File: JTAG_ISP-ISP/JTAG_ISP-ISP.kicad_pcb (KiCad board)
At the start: 2 copper layers, 23.1 x 45.1 mm, 5 parts, among them J1 Conn_02x03_Counter_Clockwise, J2 Conn_01x08, J3 Conn_01x08

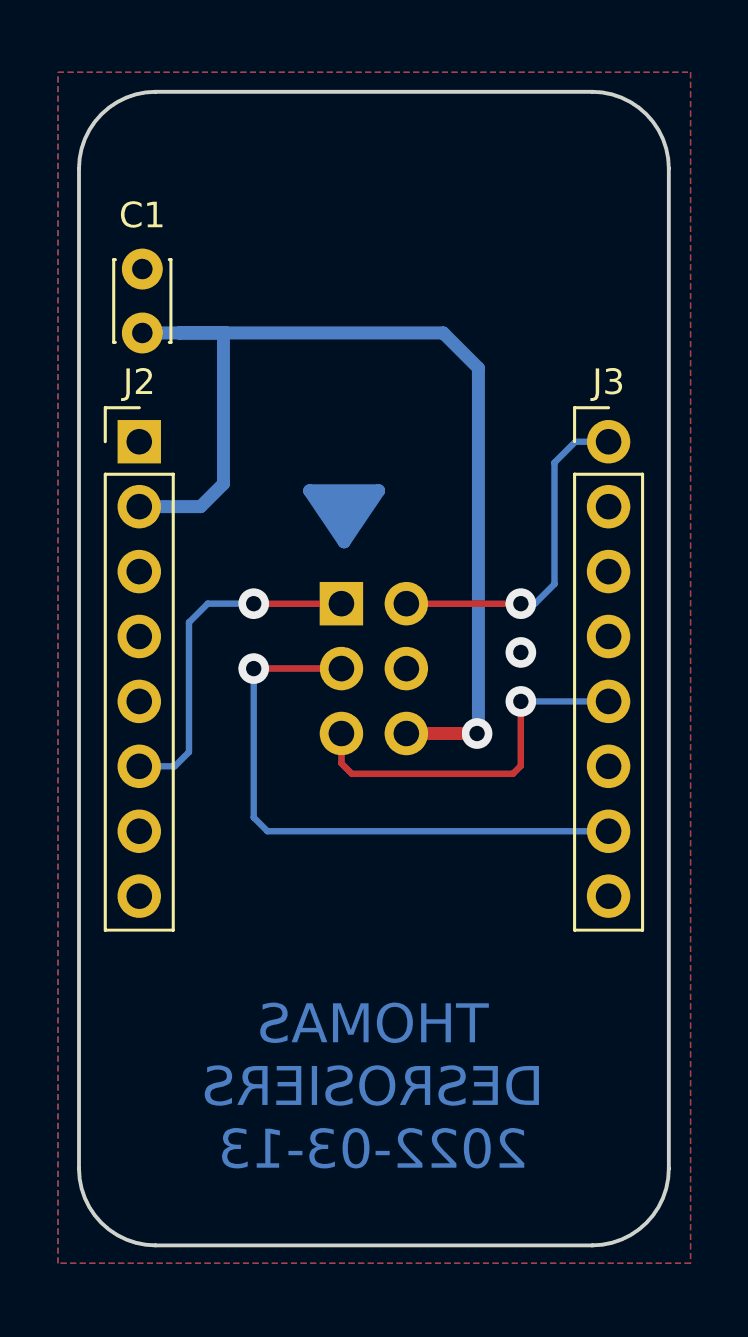
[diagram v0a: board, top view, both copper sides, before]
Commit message: + Ajout d'un trou sur chacun des 2 PCB pour pouvoir y fixer une dragone. + Ajout d'un espace de texte contenant mon nom et la date sur le PCB ISP. + Ajout d'un dossier contenant les fichiers générés pour panélisation par une application externe à KiCad. **Le circuit pour l'étage ISP est à vérifier**
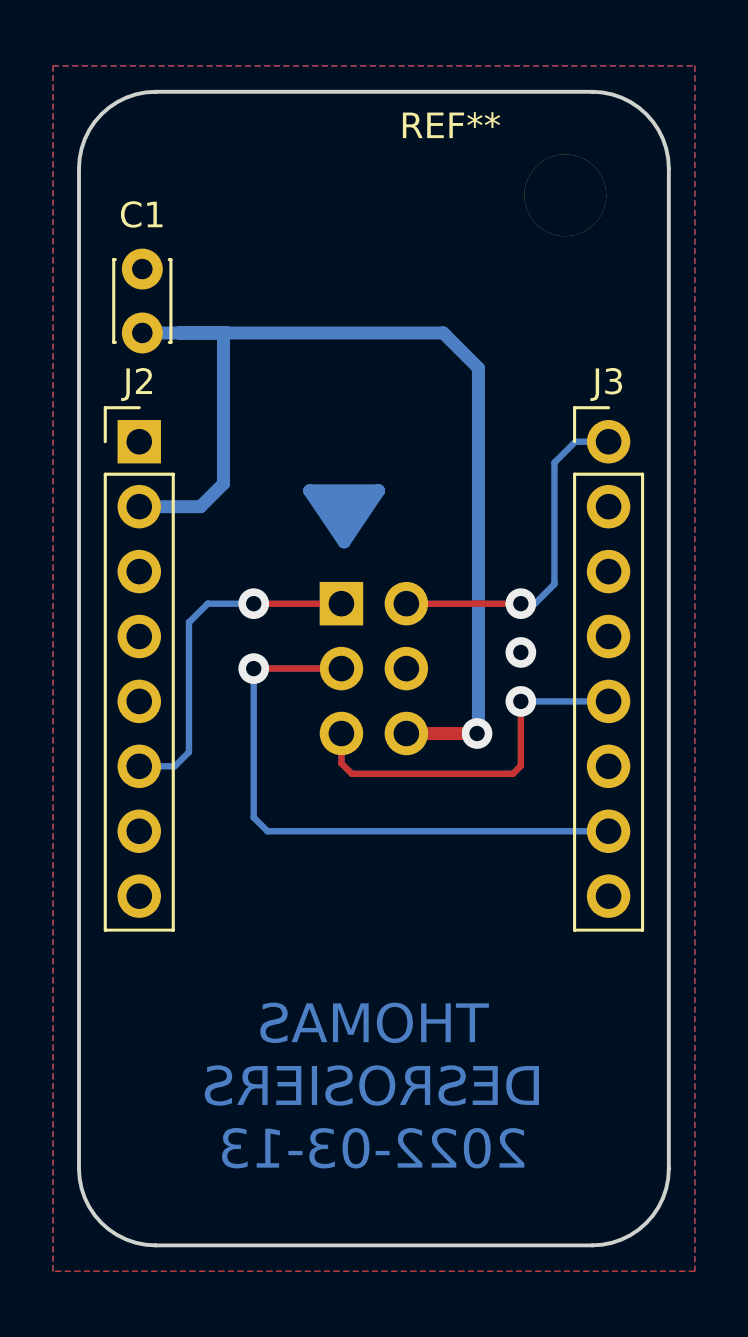
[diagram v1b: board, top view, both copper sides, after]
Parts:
- added REF**: MountingHole_3.2mm_M3, MountingHole:MountingHole_3.2mm_M3, F.Cu at (163.8, 65.9)
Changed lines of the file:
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@@
     )
     (pad_to_mask_clearance 0)
+    (aux_axis_origin 143.806012 60.797592)
+    (grid_origin 143.806012 60.797592)
     (pcbplotparams
       (layerselection 0x0001000_ffffffff)
@@
     )
   )
+  (footprint "MountingHole:MountingHole_3.2mm_M3" (layer "F.Cu")
+    (at 163.85 65.86358)
+    (descr "Mounting Hole 3.2mm, no annular, M3")
+    (tags "mounting hole 3.2mm no annular m3")
+    (attr exclude_from_pos_files exclude_from_bom)
+    (fp_text reference "REF**" (at -4.500012 -2.699989) (layer "F.SilkS")
+      (effects (font (size 1 1) (thickness 0.15)))
+    )
+    (fp_text value "MountingHole_3.2mm_M3" (at 0 4.2) (layer "F.Fab")
+      (effects (font (size 1 1) (thickness 0.15)))
+    )
+    (fp_text user "${REFERENCE}" (at -4.500012 -2.699989) (layer "F.Fab")
+      (effects (font (size 1 1) (thickness 0.15)))
+    )
+    (fp_circle (center 0 0) (end 3.2 0) (layer "Cmts.User") (width 0.15) (fill none))
+    (fp_circle (center 0 0) (end 3.45 0) (layer "F.CrtYd") (width 0.05) (fill none))
+    (pad "" thru_hole circle locked (at 0 0) (size 3.200001 3.200001) (drill 3.200001) (layers *.Cu *.Mask))
+  )
   (footprint "Connector_PinHeader_2.54mm:PinHeader_1x08_P2.54mm_Vertical" (layer "F.Cu")
     (at 165.542011 75.505767)
@@
   (gr_arc (start 167.9 103.95) (mid 167.02132 106.07132) (end 164.9 106.95) (layer "Edge.Cuts") (width 0.15))
   (gr_rect (start 167.9 61.81358) (end 144.822002 106.95) (layer "User.1") (width 1.016) (fill none))
-  (gr_rect (start 168.75 61.05) (end 144 107.65) (layer "User.2") (width 0.2) (fill none))
+  (gr_rect (start 143.806012 60.797592) (end 168.915994 107.966002) (layer "User.2") (width 0.15) (fill none))
   (gr_rect (start 167.9 61.81358) (end 144.822002 106.95) (layer "User.9") (width 0.15) (fill none))
   (gr_text "THOMAS\nDESROSIERS\n2022-03-13" (at 156.325 100.75) (layer "B.Cu")
@@
     (polygon
       (pts
-        (xy 168.75 107.65)
-        (xy 144 107.65)
-        (xy 144 61.05)
-        (xy 168.75 61.05)
+        (xy 168.915994 107.966002)
+        (xy 143.806012 107.966002)
+        (xy 143.806012 60.797592)
+        (xy 168.915994 60.797592)
       )
     )

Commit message: # [PCB] ~ Modification du PCB pour le projet ISP en fonction des nouvelles connexions sur son schéma. + Ajout de trous aux 4 coins du PCB des 2 projets (ISP & HDR). ~ Augmentation de la taille du PCB des 2 projets en ajoutant 20mills en haut et en bas. ~ Diminution de l'espace de texte (nom et date).
# [SCHÉMA]
~ Modification du schéma pour le projet ISP basé sur le fil JTAG -> ISP déjà existant.
+ Ajout de texte sur le schéma des 2 projets indiquant le nom des broches sur les headers.
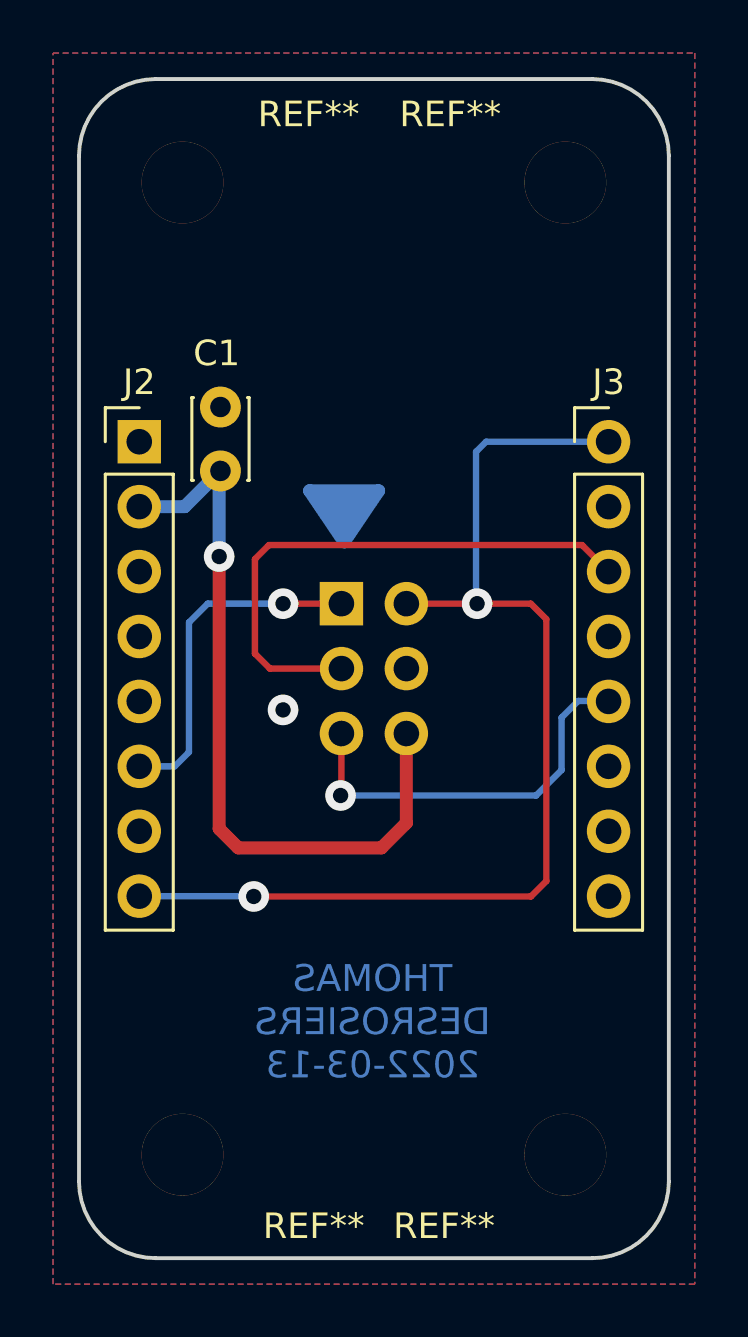
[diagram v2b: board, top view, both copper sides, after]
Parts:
- added REF**: MountingHole_3.2mm_M3, MountingHole:MountingHole_3.2mm_M3, F.Cu at (163.8, 103.4)
- added REF**: MountingHole_3.2mm_M3, MountingHole:MountingHole_3.2mm_M3, F.Cu at (148.9, 103.4)
- added REF**: MountingHole_3.2mm_M3, MountingHole:MountingHole_3.2mm_M3, F.Cu at (148.9, 65.4)
- moved C1 6.20 mm to (150.4, 76.6)
- moved REF** 0.50 mm to (163.8, 65.4)
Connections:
- J2 pad 8: unconnected-(J2-Pad8) -> SCLK
- J3 pad 3: unconnected-(J3-Pad3) -> RESET
- J3 pad 7: RESET -> unconnected-(J3-Pad7)
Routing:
- net SCLK: track 13.3 -> 43.5 mm, vias 1 -> 2
- net +5V: track 41.9 -> 29.3 mm
- net RESET: track 23.4 -> 21.8 mm, vias 1 -> 0
- net MOSI: track 14.4 -> 15.7 mm
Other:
- board size 23.1 x 45.1 mm -> 23.1 x 46.1 mm

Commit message: + Ajout d'un projet dans lequel les deux PCB sont joints.
# [PCB]
+ Ajout d'une DEL et de sa résistance en fonction des nouvelles connexions sur son schéma.
~ Déplacement du header ISP sur le côté dans le projet ISP afin de moins empiéter sur les circuits autour lorsque le shied est utilisé sur un MCU.
~ Rotation du header ISP pour être plus facilement connecté au MCU.

# [SCHÉMA]
+ Ajout d'une DEL et de sa résistance sur le broche MISO pour pour pouvoir voir quand est-ce qu'une programmation se fait.
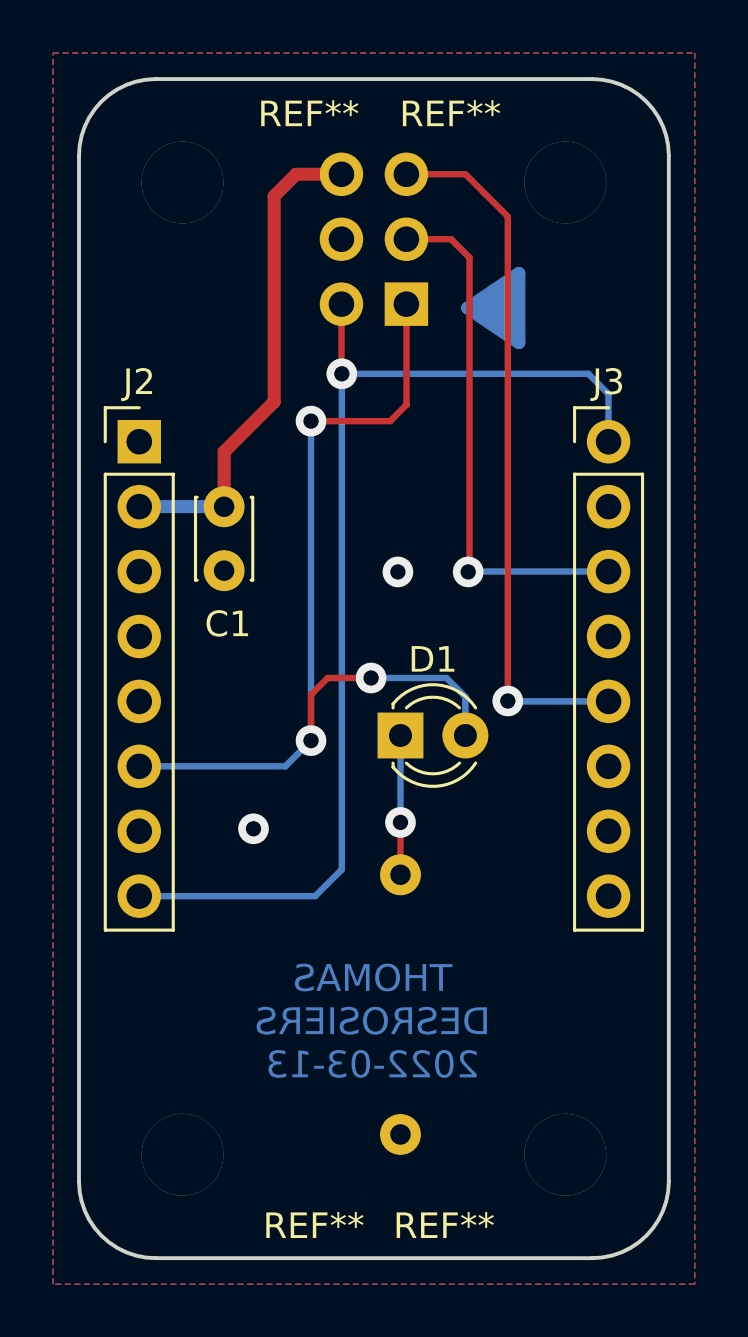
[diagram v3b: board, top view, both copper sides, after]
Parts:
- added D1: LED, LED_THT:LED_D3.0mm, F.Cu at (157.4, 87.0)
- added R1: 2k, Resistor_THT:R_Axial_DIN0207_L6.3mm_D2.5mm_P10.16mm_Horizontal, B.Cu at (157.4, 92.5)
- moved J1 12.0 mm to (157.6, 70.1), turned to 0 degrees
- moved REF** 9.48 mm to (161.3, 70.6), turned to 0 degrees
- moved C1 1.41 mm to (150.5, 78.0), turned to -90 degrees
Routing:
- net MISO: track 13.5 -> 37.7 mm, vias 1 -> 3
- net MOSI: track 15.7 -> 27.6 mm
- net +5V: track 29.3 -> 19.3 mm, vias 1 -> 0
- net Net-(D1-Pad1): track 0.00 -> 5.25 mm, vias 0 -> 1
- net RESET: track 21.8 -> 20.6 mm, vias 0 -> 1
- net SCLK: track 43.5 -> 43.1 mm, vias 2 -> 1
- net GND: vias 1 -> 2
